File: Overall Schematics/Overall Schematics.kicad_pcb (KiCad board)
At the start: 2 copper layers, 152.4 x 152.4 mm, 27 parts, among them J1 WattMeter1_Output, J2 WattMeter2_Output, J3 Intel_Buck_Converter_Input, J4 WattMeter1_Input, J5 WattMeter2_Input, M1 Stepper_Motor_bipolar, M2 Stepper_Motor_bipolar, M3 LinActuator12V, M4 LinActuator12V, M5 LinActuator12V, M6 Motor_DC, M7 Motor_DC, M8 Motor_DC, M9 Motor_DC, SW1 SW_DPST, U1 Teensy4.1, U10 VNH52019, U2 36v4SMD, U3 36v4SMD, U4 VNH52019, U5 VNH52019, U6 VNH52019, U7 VNH52019, U8 VNH52019, U9 VNH52019

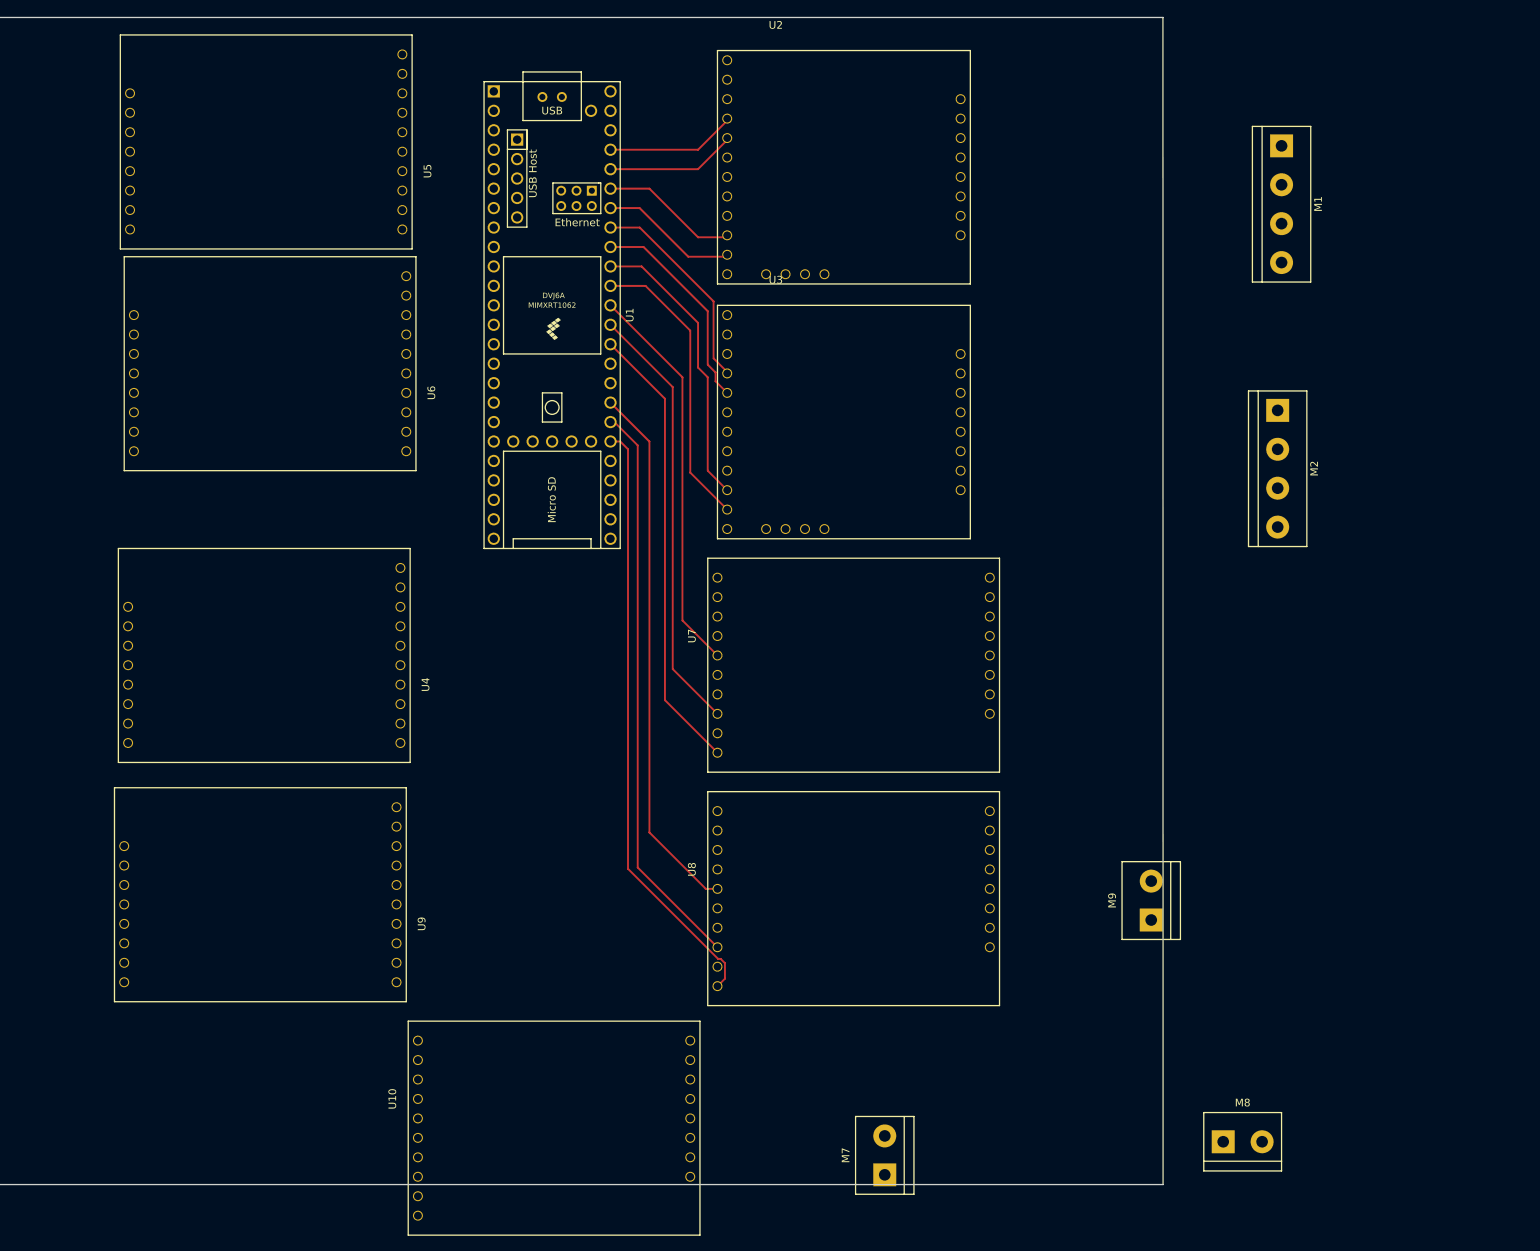
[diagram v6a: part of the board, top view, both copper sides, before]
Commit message: placement of ICs and proper pin connectors are pretty much done
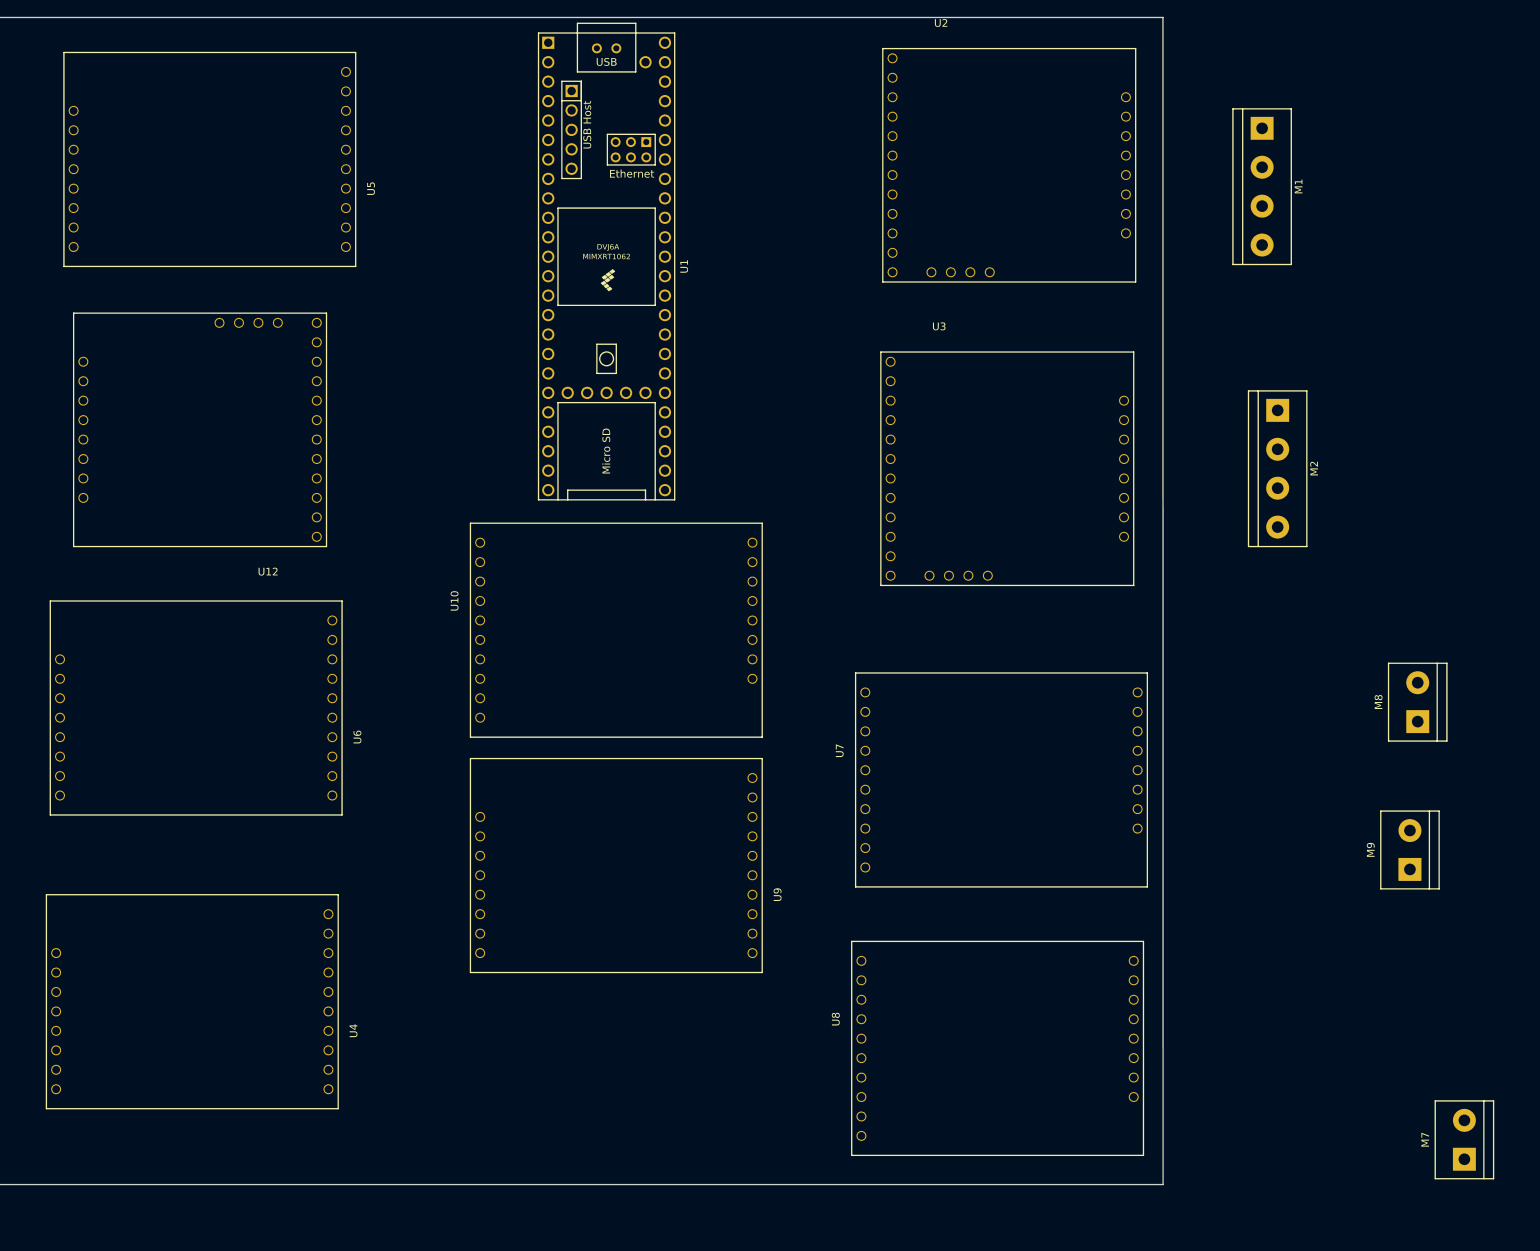
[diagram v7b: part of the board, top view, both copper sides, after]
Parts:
- added U12: 36v4SMD, Custom Footprints:StepperMotorDriver, F.Cu at (475.2, 382.5)
- moved M7 75.7 mm to (631.4, 463.8)
- moved U10 65.5 mm to (499.1, 390.9)
- moved M8 60.5 mm to (625.3, 406.7), turned to 90 degrees
- moved U9 46.6 mm to (542.3, 429.3)
- moved U4 46.2 mm to (486.9, 447.0)
- moved U6 46.0 mm to (487.4, 408.7)
- moved M9 34.4 mm to (624.3, 426.0)
- moved U8 27.1 mm to (548.9, 445.5)
- moved U7 24.4 mm to (549.4, 410.5)
- moved U3 22.2 mm to (562.9, 359.7)
- moved U2 21.6 mm to (563.1, 320.0)
- moved U1 9.53 mm to (519.4, 347.2)
- moved U5 7.71 mm to (489.2, 337.1)
- moved M1 3.42 mm to (605.0, 329.2)
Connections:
- U1 pad 10: Net-(U1-Pad10) -> STEP_3
- U1 pad 11: Net-(U1-Pad11) -> INA_5
- U1 pad 12: Net-(U1-Pad12) -> PWM_5
- U1 pad 13: Net-(U1-Pad13) -> INB_5
- U1 pad 16: PWM_5 -> INA_6
- U1 pad 20: INA_5 -> INB_6
- U1 pad 21: INB_5 -> PWM_4
- U1 pad 22: INA_6 -> INB_4
- U1 pad 23: INB_6 -> INA_4
- U1 pad 25: PWM_4 -> Net-(U1-Pad25)
- U1 pad 26: INB_4 -> Net-(U1-Pad26)
- U1 pad 27: INA_4 -> Net-(U1-Pad27)
- U1 pad 7: Net-(U1-Pad7) -> RESET_3
- U1 pad 8: Net-(U1-Pad8) -> SLEEP_3
- U1 pad 9: Net-(U1-Pad9) -> DIR_3
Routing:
- net INA_2: track 78.7 -> 0.00 mm
- net PWM_2: track 74.7 -> 0.00 mm
- net INB_2: track 70.2 -> 0.00 mm
- net INA_1: track 59.1 -> 0.00 mm
- net PWM_1: track 56.6 -> 0.00 mm
- net INB_1: track 51.5 -> 0.00 mm
- net RESET_2: track 38.2 -> 0.00 mm
- net SLEEP_2: track 37.9 -> 0.00 mm
- net DIR_2: track 27.9 -> 0.00 mm
- net STEP_2: track 27.6 -> 0.00 mm
- net SLEEP_1: track 17.9 -> 0.00 mm
- net RESET_1: track 17.9 -> 0.00 mm
- net STEP_1: track 16.8 -> 0.00 mm
- net DIR_1: track 16.8 -> 0.00 mm

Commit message: finished routing main ICs, have to figure out power routing, vary track width
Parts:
- M1, M2, M3, M4, M5, M6, M7, M8, M9: moved to B.Cu
- moved M7 78.0 mm to (608.1, 389.4), turned to 270 degrees
- moved M9 18.1 mm to (610.1, 437.1), turned to 270 degrees
- moved M8 16.0 mm to (609.3, 406.7), turned to 270 degrees
- moved M6 8.48 mm to (423.9, 431.5), turned to 90 degrees
- moved M2 4.10 mm to (608.6, 362.2)
- moved M5 3.09 mm to (426.0, 361.4), turned to 90 degrees
- moved M4 2.96 mm to (425.7, 326.6), turned to 90 degrees
- moved M1 2.40 mm to (607.1, 330.5)
- turned M3 to 90 degrees
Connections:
- U1 pad 14: INA_3 -> INA_6
- U1 pad 16: INA_6 -> PWM_6
- U1 pad 17: PWM_6 -> LIN_SIGNAL1
- U1 pad 18: LIN_SIGNAL1 -> LIN_SIGNAL2
- U1 pad 19: LIN_SIGNAL2 -> LIN_SIGNAL3
- U1 pad 27: Net-(U1-Pad27) -> INA_3
- U1 pad 33: LIN_SIGNAL3 -> Net-(U1-Pad33)
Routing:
- net INA_2: track 0.00 -> 107.7 mm
- net PWM_2: track 0.00 -> 105.1 mm
- net INB_2: track 0.00 -> 100.0 mm
- net PWM_6: track 0.00 -> 94.3 mm
- net INA_6: track 0.00 -> 93.4 mm
- net INB_6: track 0.00 -> 92.9 mm
- net INA_1: track 0.00 -> 85.5 mm
- net PWM_1: track 0.00 -> 83.0 mm
- net INB_1: track 0.00 -> 77.9 mm
- net INB_5: track 0.00 -> 69.3 mm
- net INB_3: track 0.00 -> 67.5 mm
- net PWM_5: track 0.00 -> 64.3 mm
- net INA_5: track 0.00 -> 62.8 mm
- net PWM_3: track 0.00 -> 59.5 mm
- net RESET_2: track 0.00 -> 53.9 mm
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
